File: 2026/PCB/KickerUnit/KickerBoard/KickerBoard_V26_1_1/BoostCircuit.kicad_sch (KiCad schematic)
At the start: 28 parts, among them Q1 FDS2582, T1 750032052, U1 LT3751UFD

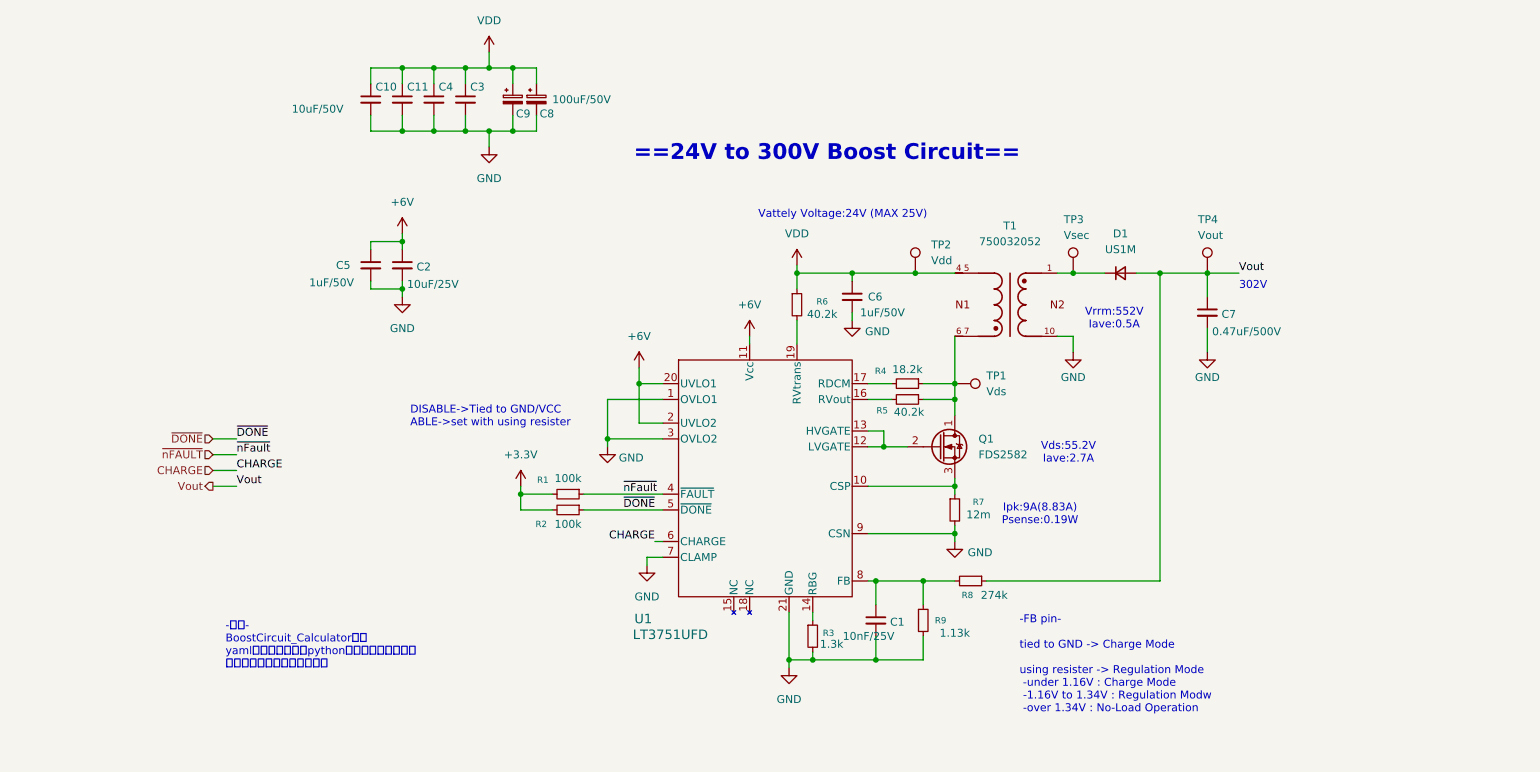
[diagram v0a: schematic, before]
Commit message: 6.5V降圧DCDCの追加
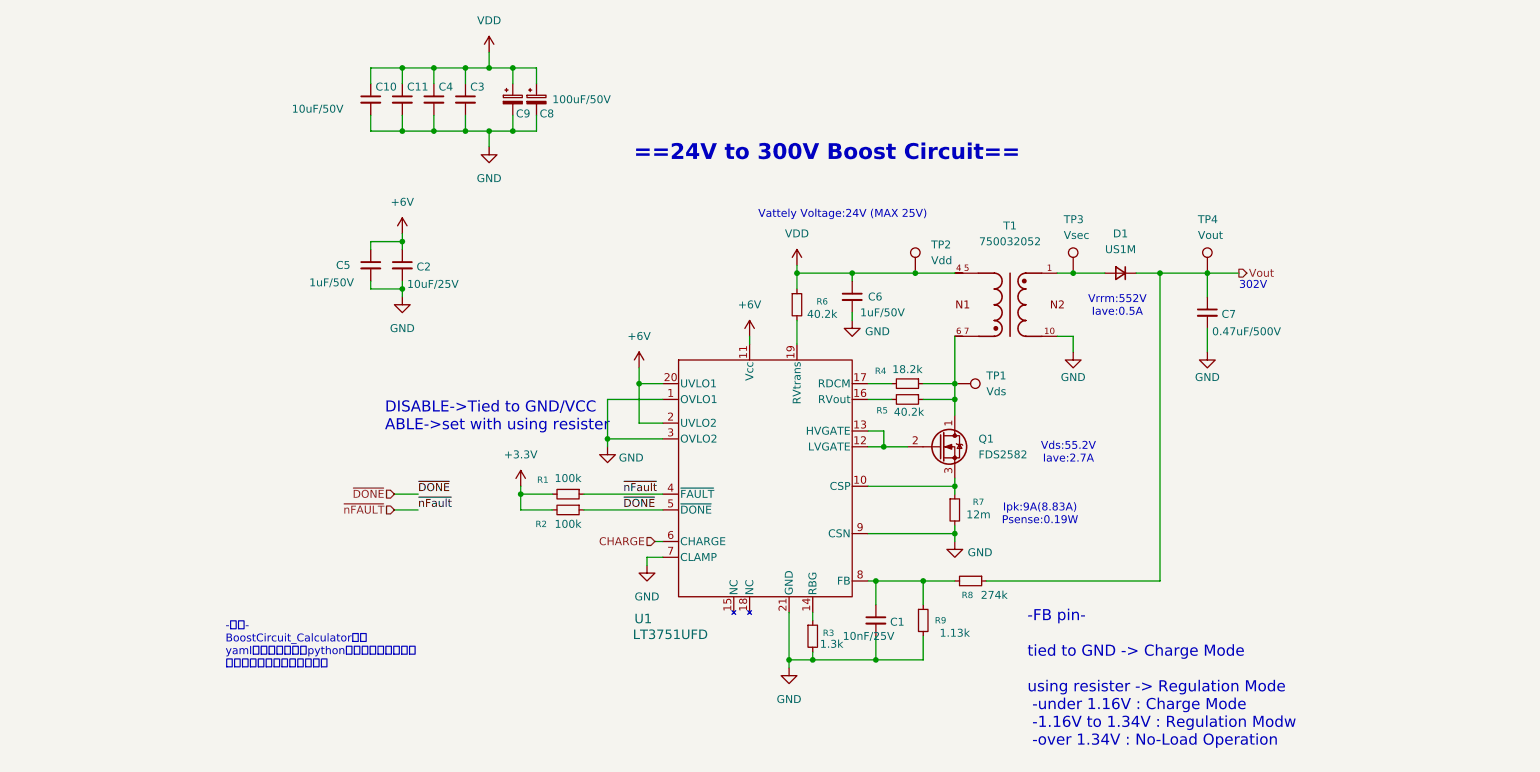
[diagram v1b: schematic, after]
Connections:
- net Vout: now also D1.1 (K); no longer D1.2 (A)
- net at T1.1, TP3.1: now also D1.2 (A); no longer D1.1 (K)
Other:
- moved on the sheet: D1
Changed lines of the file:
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@@
 	(text "DISABLE->Tied to GND/VCC\nABLE->set with using resister"
 		(exclude_from_sim no)
-		(at 87.63 92.964 0)
+		(at 83.566 92.964 0)
 		(effects
 			(font
-				(size 1.27 1.27)
+				(face "Arial")
+				(size 1.778 1.778)
+				(color 72 72 72 1)
 			)
 			(justify left)
@@
 		(effects
 			(font
+				(face "Arial")
 				(size 2.54 2.54)
 				(thickness 0.508)
 				(bold yes)
+				(color 72 72 72 1)
 			)
 		)
@@
 	(text "Vrrm:552V\nIave:0.5A"
 		(exclude_from_sim no)
-		(at 200.914 77.216 0)
+		(at 201.422 75.184 0)
 		(effects
 			(font
+				(face "Arial")
 				(size 1.27 1.27)
+				(color 72 72 72 1)
 			)
 		)
@@
 	(text "-FB pin-\n\ntied to GND -> Charge Mode\n\nusing resister -> Regulation Mode\n -under 1.16V : Charge Mode\n -1.16V to 1.34V : Regulation Modw\n -over 1.34V : No-Load Operation"
 		(exclude_from_sim no)
-		(at 185.674 132.842 0)
+		(at 186.944 135.128 0)
 		(effects
 			(font
-				(size 1.27 1.27)
+				(face "Arial")
+				(size 1.778 1.778)
+				(color 72 72 72 1)
 			)
 			(justify left)
@@
 		(effects
 			(font
+				(face "Arial")
 				(size 1.27 1.27)
+				(color 72 72 72 1)
 			)
 		)
@@
 		(effects
 			(font
+				(face "Arial")
 				(size 1.27 1.27)
+				(color 72 72 72 1)
 			)
 		)
@@
 		(effects
 			(font
+				(face "Arial")
 				(size 1.27 1.27)
+				(color 72 72 72 1)
 			)
 		)
@@
 		(effects
 			(font
+				(face "Arial")
 				(size 1.27 1.27)
+				(color 72 72 72 1)
 			)
 		)
@@
 	(wire
 		(pts
-			(xy 59.69 101.6) (xy 55.88 101.6)
-		)
-		(stroke
-			(width 0)
-			(type default)
-		)
-	)
-	(wire
-		(pts
 			(xy 100.33 46.99) (xy 104.14 46.99)
 		)
@@
 	(wire
 		(pts
-			(xy 59.69 99.06) (xy 55.88 99.06)
+			(xy 88.9 107.95) (xy 85.09 107.95)
 		)
 		(stroke
@@
 	(wire
 		(pts
-			(xy 59.69 104.14) (xy 55.88 104.14)
-		)
-		(stroke
-			(width 0)
-			(type default)
-		)
-	)
-	(wire
-		(pts
 			(xy 175.26 90.17) (xy 175.26 92.71)
 		)
@@
 	(wire
 		(pts
-			(xy 59.69 96.52) (xy 55.88 96.52)
+			(xy 88.9 105.41) (xy 85.09 105.41)
 		)
 		(stroke
@@
 	)
 	(label "~{nFault}"
-		(at 59.69 99.06 0)
-		(effects
-			(font
-				(size 1.27 1.27)
-			)
-			(justify left bottom)
-		)
-	)
-	(label "CHARGE"
-		(at 127 113.03 180)
-		(effects
-			(font
-				(size 1.27 1.27)
-			)
-			(justify right bottom)
-		)
-	)
-	(label "Vout"
-		(at 59.69 104.14 0)
+		(at 88.9 107.95 0)
 		(effects
 			(font
@@
 		)
 	)
-	(label "Vout"
-		(at 220.98 69.85 0)
-		(effects
-			(font
-				(size 1.27 1.27)
-			)
-			(justify left bottom)
-		)
-	)
 	(label "~{DONE}"
-		(at 59.69 96.52 0)
+		(at 88.9 105.41 0)
 		(effects
 			(font
@@
 		)
 	)
-	(label "CHARGE"
-		(at 59.69 101.6 0)
-		(effects
-			(font
-				(size 1.27 1.27)
-			)
-			(justify left bottom)
-		)
-	)
-	(hierarchical_label "Vout"
-		(shape output)
-		(at 55.88 104.14 180)
+	(hierarchical_label "CHARGE"
+		(shape input)
+		(at 127 113.03 180)
 		(effects
 			(font
@@
 	(hierarchical_label "~{DONE}"
 		(shape input)
-		(at 55.88 96.52 180)
+		(at 85.09 105.41 180)
 		(effects
 			(font
@@
 		)
 	)
-	(hierarchical_label "CHARGE"
+	(hierarchical_label "~{nFAULT}"
 		(shape input)
-		(at 55.88 101.6 180)
+		(at 85.09 107.95 180)
 		(effects
 			(font
@@
 		)
 	)
-	(hierarchical_label "~{nFAULT}"
-		(shape input)
-		(at 55.88 99.06 180)
+	(hierarchical_label "Vout"
+		(shape output)
+		(at 220.98 69.85 0)
 		(effects
 			(font
 				(size 1.27 1.27)
 			)
-			(justify right)
+			(justify left)
 		)
 	)
@@
 	(symbol
 		(lib_id "Device:D_Small")
-		(at 201.93 69.85 0)
+		(at 201.93 69.85 180)
 		(unit 1)
 		(exclude_from_sim no)

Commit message: 回路図完成
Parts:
- removed R1, R2: 100k, symbol Device:R_Small
- added C26, C27: 1200uF/350V, Capacitor_THT:CP_Radial_D30.0mm_P10.00mm_SnapIn, symbol Device:C_Polarized_Small
- added D5, D6: LED, KickerUnit_LIB_FTP:LED, symbol Device:LED_Small
- added Q1: Q_NMOS_GDS, Package_TO_SOT_SMD:TO-252-3_TabPin2, symbol Transistor_FET:Q_NMOS_GDS
- added R10, R11, R8, R9: 30k/1W, Resistor_SMD:R_1206_3216Metric_Pad1.30x1.75mm_HandSolder, symbol Device:R_Small
- added R14, R15: 1k, Resistor_SMD:R_0603_1608Metric_Pad0.98x0.95mm_HandSolder, symbol Device:R_Small
- added TP5: GND, TestPoint:TestPoint_THTPad_D2.5mm_Drill1.2mm, symbol Connector:TestPoint
- C16: renamed from C10; footprint (none) -> Capacitor_SMD:C_0805_2012Metric_Pad1.18x1.45mm_HandSolder
- C17: renamed from C11; footprint (none) -> Capacitor_SMD:C_0805_2012Metric_Pad1.18x1.45mm_HandSolder
- C18: renamed from C4; footprint (none) -> Capacitor_SMD:C_0805_2012Metric_Pad1.18x1.45mm_HandSolder
- C19: renamed from C3; footprint (none) -> Capacitor_SMD:C_0805_2012Metric_Pad1.18x1.45mm_HandSolder
- C20: renamed from C9; value 100uF/50V -> 100uF/35V; footprint (none) -> Capacitor_THT:CP_Radial_D6.3mm_P2.50mm
- C21: renamed from C8; value 100uF/50V -> 100uF/35V; footprint (none) -> Capacitor_THT:CP_Radial_D6.3mm_P2.50mm
- C22: renamed from C5; footprint Resistor_SMD:R_0805_2012Metric_Pad1.20x1.40mm_HandSolder -> Capacitor_SMD:C_0603_1608Metric_Pad1.08x0.95mm_HandSolder
- C23: renamed from C2; footprint Resistor_SMD:R_0805_2012Metric_Pad1.20x1.40mm_HandSolder -> Capacitor_SMD:C_0603_1608Metric_Pad1.08x0.95mm_HandSolder
- C24: renamed from C6; footprint Resistor_SMD:R_0805_2012Metric_Pad1.20x1.40mm_HandSolder -> Capacitor_SMD:C_0603_1608Metric_Pad1.08x0.95mm_HandSolder
- C28: renamed from C1; footprint (none) -> Capacitor_SMD:C_0402_1005Metric_Pad0.74x0.62mm_HandSolder
- Q2: renamed from Q1; footprint KickerUnit_LIB_SYM:FDS2582(SOIC8) -> KickerUnit_LIB_FTP:FDS2582(SOIC8)
- R12: renamed from R4; footprint (none) -> Resistor_SMD:R_0603_1608Metric_Pad0.98x0.95mm_HandSolder
- R13: renamed from R5; footprint (none) -> Resistor_SMD:R_0603_1608Metric_Pad0.98x0.95mm_HandSolder
- R17: renamed from R8; value 274k -> 280k; footprint (none) -> Resistor_SMD:R_0603_1608Metric_Pad0.98x0.95mm_HandSolder
- R18: renamed from R9; value 1.13k -> 1k; footprint (none) -> Resistor_SMD:R_0603_1608Metric_Pad0.98x0.95mm_HandSolder
- R19: renamed from R3; footprint (none) -> Resistor_SMD:R_0603_1608Metric_Pad0.98x0.95mm_HandSolder
- R7: renamed from R6; footprint (none) -> Resistor_SMD:R_0603_1608Metric_Pad0.98x0.95mm_HandSolder
- T1: footprint KickerUnit_LIB_SYM:WE-FB3751 -> KickerUnit_LIB_FTP:WE-FB3751
- TP1: renamed from TP2; footprint (none) -> TestPoint:TestPoint_Pad_2.0x2.0mm
- TP2: renamed from TP3; footprint (none) -> TestPoint:TestPoint_Pad_2.0x2.0mm
- TP3: renamed from TP4; footprint (none) -> TestPoint:TestPoint_Pad_2.0x2.0mm
- TP4: renamed from TP1; footprint (none) -> TestPoint:TestPoint_Pad_2.0x2.0mm
- U4: renamed from U1; footprint KickerUnit_LIB_SYM:QFN-20-1EP_LT3751UFD -> KickerUnit_LIB_FTP:QFN-20-1EP_LT3751UFD
- renumbered C7 to C25, D1 to D4, R7 to R16
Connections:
- net +3.3V: now also R14.1, R15.1
- net GND: now also C26.2, C27.2, Q1.3 (S), TP5.1
- net Vout: now also C26.1, C27.1, R10.1, R11.1, R8.1, R9.1
- net ~{DONE}: now also D5.1 (K)
- net ~{nFAULT}: now also D6.1 (K)
- new net: Q1.2 (D), R10.2, R11.2, R8.2, R9.2
- new net: D6.2 (A), R15.2
- new net: D5.2 (A), R14.2
- new net DISCHARGE: Q1.1 (G)
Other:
- note added: "Ipk:9A(8.83A) Psense: 1W(0 .19W)"
- note added: "when Fault LED ON, nFault 0V when Done LED ON, nDone 0V"
- note removed: "Ipk:9A(8.83A) Psense:0.19W"
- moved on the sheet: C16, C17, C18, C19, C20, C21, C22, C23, C24, C25, C28, D4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

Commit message: アートワークほぼ完了
ビアとシルクのみ
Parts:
- removed TP2: Vsec, TestPoint:TestPoint_Pad_2.0x2.0mm, symbol Connector:TestPoint
- renumbered TP3 to TP2, TP4 to TP3, TP5 to TP4
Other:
- moved on the sheet: C21
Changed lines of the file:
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@@
 	)
 	(junction
-		(at 160.02 71.12)
-		(diameter 0)
-		(color 0 0 0 0)
-	)
-	(junction
 		(at 213.36 87.63)
 		(diameter 0)
@@
 	(wire
 		(pts
-			(xy 160.02 71.12) (xy 157.48 71.12)
-		)
-		(stroke
-			(width 0)
-			(type default)
-		)
-	)
-	(wire
-		(pts
 			(xy 46.99 40.64) (xy 46.99 38.1)
 		)
@@
 	(wire
 		(pts
-			(xy 69.85 48.26) (xy 73.66 48.26)
+			(xy 69.85 48.26) (xy 74.93 48.26)
 		)
 		(stroke
@@
 	(wire
 		(pts
-			(xy 73.66 40.64) (xy 73.66 38.1)
+			(xy 74.93 40.64) (xy 74.93 38.1)
 		)
 		(stroke
@@
 	(wire
 		(pts
-			(xy 69.85 38.1) (xy 73.66 38.1)
+			(xy 69.85 38.1) (xy 74.93 38.1)
 		)
 		(stroke
@@
 	(wire
 		(pts
-			(xy 165.1 71.12) (xy 160.02 71.12)
+			(xy 157.48 71.12) (xy 165.1 71.12)
 		)
 		(stroke
@@
 	(wire
 		(pts
-			(xy 73.66 48.26) (xy 73.66 45.72)
+			(xy 74.93 48.26) (xy 74.93 45.72)
 		)
 		(stroke
@@
 	)
 	(symbol
-		(lib_id "Connector:TestPoint")
-		(at 160.02 71.12 0)
-		(unit 1)
-		(exclude_from_sim no)
-		(in_bom yes)
-		(on_board yes)
-		(dnp no)
-		(property "Reference" "TP2"
-			(at 158.496 62.484 0)
-			(effects
-				(font
-					(size 1.27 1.27)
-				)
-				(justify left)
-			)
-		)
-		(property "Value" "Vsec"
-			(at 158.496 65.024 0)
-			(effects
-				(font
-					(size 1.27 1.27)
-				)
-				(justify left)
-			)
-		)
-		(property "Footprint" "TestPoint:TestPoint_Pad_2.0x2.0mm"
-			(at 165.1 71.12 0)
-			(effects
-				(font
-					(size 1.27 1.27)
-				)
-				(hide yes)
-			)
-		)
-		(property "Datasheet" "~"
-			(at 165.1 71.12 0)
-			(effects
-				(font
-					(size 1.27 1.27)
-				)
-				(hide yes)
-			)
-		)
-		(property "Description" ""
-			(at 160.02 71.12 0)
-			(effects
-				(font
-					(size 1.27 1.27)
-				)
-				(hide yes)
-			)
-		)
-		(pin "1"
-		)
-		(instances
-			(project "KickerBoard_V26_1_1"
-				(path "/8c63cf69-5ffc-4db2-9a00-dda132db51ca/a55bac2c-0983-42ce-9d17-5e08fcd2bf34"
-					(reference "TP2")
-					(unit 1)
-				)
-			)
-		)
-	)
-	(symbol
 		(lib_id "KickerUnit_LIB_SYM:LT3751UFD")
 		(at 111.76 100.33 0)
@@
 		(dnp no)
 		(fields_autoplaced yes)
-		(property "Reference" "#PWR036"
+		(property "Reference" "#PWR037"
 			(at 69.85 92.71 0)
 			(effects
@@
 			(project "KickerBoard_V26_1_1"
 				(path "/8c63cf69-5ffc-4db2-9a00-dda132db51ca/a55bac2c-0983-42ce-9d17-5e08fcd2bf34"
-					(reference "#PWR036")
+					(reference "#PWR037")
 					(unit 1)
 				)
@@
 		(dnp no)
 		(fields_autoplaced yes)
-		(property "Reference" "TP5"
+		(property "Reference" "TP4"
 			(at 110.998 128.27 90)
 			(effects
@@
 			(project "KickerBoard_V26_1_1"
 				(path "/8c63cf69-5ffc-4db2-9a00-dda132db51ca/a55bac2c-0983-42ce-9d17-5e08fcd2bf34"
-					(reference "TP5")
+					(reference "TP4")
 					(unit 1)
 				)
@@
 		(on_board yes)
 		(dnp no)
-		(property "Reference" "#PWR031"
+		(property "Reference" "#PWR032"
 			(at 124.46 85.09 0)
 			(effects
@@
 			(project "KickerBoard_V26_1_1"
 				(path "/8c63cf69-5ffc-4db2-9a00-dda132db51ca/a55bac2c-0983-42ce-9d17-5e08fcd2bf34"
-					(reference "#PWR031")
+					(reference "#PWR032")
 					(unit 1)
 				)
@@
 		(dnp no)
 		(fields_autoplaced yes)
-		(property "Reference" "#PWR042"
+		(property "Reference" "#PWR043"
 			(at 114.3 140.97 0)
 			(effects
@@
 			(project "KickerBoard_V26_1_1"
 				(path "/8c63cf69-5ffc-4db2-9a00-dda132db51ca/a55bac2c-0983-42ce-9d17-5e08fcd2bf34"
-					(reference "#PWR042")
+					(reference "#PWR043")
 					(unit 1)
 				)
@@
 		(dnp no)
 		(fields_autoplaced yes)
-		(property "Reference" "#PWR035"
+		(property "Reference" "#PWR036"
 			(at 90.17 90.17 0)
 			(effects
@@
 			(project "KickerBoard_V26_1_1"
 				(path "/8c63cf69-5ffc-4db2-9a00-dda132db51ca/a55bac2c-0983-42ce-9d17-5e08fcd2bf34"
-					(reference "#PWR035")
+					(reference "#PWR036")
 					(unit 1)
 				)
@@
 		(on_board yes)
 		(dnp no)
-		(property "Reference" "#PWR034"
+		(property "Reference" "#PWR035"
 			(at 181.61 90.17 0)
 			(effects
@@
 			(project "KickerBoard_V26_1_1"
 				(path "/8c63cf69-5ffc-4db2-9a00-dda132db51ca/a55bac2c-0983-42ce-9d17-5e08fcd2bf34"
-					(reference "#PWR034")
+					(reference "#PWR035")
 					(unit 1)
 				)
@@
 		(dnp no)
 		(fields_autoplaced yes)
-		(property "Reference" "#PWR028"
+		(property "Reference" "#PWR029"
 			(at 49.53 62.23 0)
 			(effects
@@
 			(project "KickerBoard_V26_1_1"
 				(path "/8c63cf69-5ffc-4db2-9a00-dda132db51ca/a55bac2c-0983-42ce-9d17-5e08fcd2bf34"
-					(reference "#PWR028")
+					(reference "#PWR029")
 					(unit 1)
 				)
@@
 		(dnp no)
 		(fields_autoplaced yes)
-		(property "Reference" "#PWR032"
+		(property "Reference" "#PWR033"
 			(at 107.95 85.09 0)
 			(effects
@@
 			(project "KickerBoard_V26_1_1"
 				(path "/8c63cf69-5ffc-4db2-9a00-dda132db51ca/a55bac2c-0983-42ce-9d17-5e08fcd2bf34"
-					(reference "#PWR032")
+					(reference "#PWR033")
 					(unit 1)
 				)
@@
 		(on_board yes)
 		(dnp no)
-		(property "Reference" "#PWR033"
+		(property "Reference" "#PWR034"
 			(at 160.02 90.17 0)
 			(effects
@@
 			(project "KickerBoard_V26_1_1"
 				(path "/8c63cf69-5ffc-4db2-9a00-dda132db51ca/a55bac2c-0983-42ce-9d17-5e08fcd2bf34"
-					(reference "#PWR033")
+					(reference "#PWR034")
 					(unit 1)
 				)
@@
 		(on_board yes)
 		(dnp no)
-		(property "Reference" "#PWR038"
+		(property "Reference" "#PWR039"
 			(at 85.09 105.41 0)
 			(effects
@@
 			(project "KickerBoard_V26_1_1"
 				(path "/8c63cf69-5ffc-4db2-9a00-dda132db51ca/a55bac2c-0983-42ce-9d17-5e08fcd2bf34"
-					(reference "#PWR038")
+					(reference "#PWR039")
 					(unit 1)
 				)
@@
 		(dnp no)
 		(fields_autoplaced yes)
-		(property "Reference" "#PWR027"
+		(property "Reference" "#PWR028"
 			(at 66.04 57.15 0)
 			(effects
@@
 			(project "KickerBoard_V26_1_1"
 				(path "/8c63cf69-5ffc-4db2-9a00-dda132db51ca/a55bac2c-0983-42ce-9d17-5e08fcd2bf34"
-					(reference "#PWR027")
+					(reference "#PWR028")
 					(unit 1)
 				)
@@
 		(on_board yes)
 		(dnp no)
-		(property "Reference" "#PWR040"
+		(property "Reference" "#PWR041"
 			(at 140.97 120.65 0)
 			(effects
@@
 			(project "KickerBoard_V26_1_1"
 				(path "/8c63cf69-5ffc-4db2-9a00-dda132db51ca/a55bac2c-0983-42ce-9d17-5e08fcd2bf34"
-					(reference "#PWR040")
+					(reference "#PWR041")
 					(unit 1)
 				)
@@
 		(on_board yes)
 		(dnp no)
-		(property "Reference" "TP3"
+		(property "Reference" "TP2"
 			(at 180.086 62.484 0)
 			(effects
@@
 			(project "KickerBoard_V26_1_1"
 				(path "/8c63cf69-5ffc-4db2-9a00-dda132db51ca/a55bac2c-0983-42ce-9d17-5e08fcd2bf34"
-					(reference "TP3")
+					(reference "TP2")
 					(unit 1)
 				)
@@
 		(dnp no)
 		(fields_autoplaced yes)
-		(property "Reference" "#PWR030"
+		(property "Reference" "#PWR031"
 			(at 115.57 73.66 0)
 			(effects
@@
 			(project "KickerBoard_V26_1_1"
 				(path "/8c63cf69-5ffc-4db2-9a00-dda132db51ca/a55bac2c-0983-42ce-9d17-5e08fcd2bf34"
-					(reference "#PWR030")
+					(reference "#PWR031")
 					(unit 1)
 				)
@@
 		(dnp no)
 		(fields_autoplaced yes)
-		(property "Reference" "#PWR029"
+		(property "Reference" "#PWR030"
 			(at 49.53 74.93 0)
 			(effects
@@
 			(project "KickerBoard_V26_1_1"
 				(path "/8c63cf69-5ffc-4db2-9a00-dda132db51ca/a55bac2c-0983-42ce-9d17-5e08fcd2bf34"
-					(reference "#PWR029")
+					(reference "#PWR030")
 					(unit 1)
 				)
@@
 		(on_board yes)
 		(dnp no)
-		(property "Reference" "#PWR039"
+		(property "Reference" "#PWR040"
 			(at 213.36 110.49 0)
 			(effects
@@
 			(project "KickerBoard_V26_1_1"
 				(path "/8c63cf69-5ffc-4db2-9a00-dda132db51ca/a55bac2c-0983-42ce-9d17-5e08fcd2bf34"
-					(reference "#PWR039")
+					(reference "#PWR040")
 					(unit 1)
 				)
@@
 		(on_board yes)
 		(dnp no)
-		(property "Reference" "#PWR037"
+		(property "Reference" "#PWR038"
 			(at 242.57 96.52 0)
 			(effects
@@
 			(project "KickerBoard_V26_1_1"
 				(path "/8c63cf69-5ffc-4db2-9a00-dda132db51ca/a55bac2c-0983-42ce-9d17-5e08fcd2bf34"
-					(reference "#PWR037")
+					(reference "#PWR038")
 					(unit 1)
 				)
@@
 		(dnp no)
 		(fields_autoplaced yes)
-		(property "Reference" "#PWR026"
+		(property "Reference" "#PWR027"
 			(at 66.04 39.37 0)
 			(effects
@@
 			(project "KickerBoard_V26_1_1"
 				(path "/8c63cf69-5ffc-4db2-9a00-dda132db51ca/a55bac2c-0983-42ce-9d17-5e08fcd2bf34"
-					(reference "#PWR026")
+					(reference "#PWR027")
 					(unit 1)
 				)
@@
 		(dnp no)
 		(fields_autoplaced yes)
-		(property "Reference" "#PWR041"
+		(property "Reference" "#PWR042"
 			(at 91.44 124.46 0)
 			(effects
@@
 			(project "KickerBoard_V26_1_1"
 				(path "/8c63cf69-5ffc-4db2-9a00-dda132db51ca/a55bac2c-0983-42ce-9d17-5e08fcd2bf34"
-					(reference "#PWR041")
+					(reference "#PWR042")
 					(unit 1)
 				)
@@
 		(dnp no)
 		(fields_autoplaced yes)
-		(property "Reference" "TP4"
+		(property "Reference" "TP3"
 			(at 146.05 87.6299 90)
 			(effects
@@
 			(project "KickerBoard_V26_1_1"
 				(path "/8c63cf69-5ffc-4db2-9a00-dda132db51ca/a55bac2c-0983-42ce-9d17-5e08fcd2bf34"
-					(reference "TP4")
+					(reference "TP3")
 					(unit 1)
 				)
@@
 	(symbol
 		(lib_id "Device:C_Polarized_Small")
-		(at 73.66 43.18 0)
+		(at 74.93 43.18 0)
 		(unit 1)
 		(exclude_from_sim no)
@@
 		(dnp no)
 		(property "Reference" "C21"
-			(at 74.168 45.466 0)
+			(at 75.438 45.466 0)
 			(effects
 				(font
@@
 		)
 		(property "Value" "100uF/35V"
-			(at 76.2 43.18 0)
+			(at 77.47 43.18 0)
 			(effects
 				(font
@@
 		)
 		(property "Footprint" "Capacitor_THT:CP_Radial_D6.3mm_P2.50mm"
-			(at 73.66 43.18 0)
+			(at 74.93 43.18 0)
 			(effects
 				(font
@@
 		)
 		(property "Datasheet" "https://www.digikey.jp/ja/products/detail/rubycon/35ZLH100MEFC6-3X11/3134256"
-			(at 73.66 43.18 0)
+			(at 74.93 43.18 0)
 			(effects
 				(font
@@
 		)
 		(property "Description" "35ZLH100MEFC6.3X11"
-			(at 73.66 43.18 0)
+			(at 74.93 43.18 0)
 			(effects
 				(font
